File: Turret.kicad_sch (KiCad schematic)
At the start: 0 parts

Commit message: Update schematic
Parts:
- added Feeder1, L_Flywheel_ESC, R_Flywheel_ESC1, Waterwheel1: ~, symbol Robomaster_Library:motor_speed_controller
- added J1: Conn_01x04_Pin, symbol Connector:Conn_01x04_Pin
- added J12, J2, J4, J6, J8: Conn_01x02_Pin, Connector_AMASS:AMASS_XT30U-F_1x02_P5.0mm_Vertical, symbol Connector:Conn_01x02_Pin
- added J13, J3, J5, J7, J9: Conn_01x02_Pin, Connector_JST:JST_GH_BM02B-GHS-TBT_1x02-1MP_P1.25mm_Vertical, symbol Connector:Conn_01x02_Pin
- added SMM1: ~, symbol Robomaster_Library:SMM
- added pitch_motor2: ~, symbol Robomaster_Library:pitch_motor
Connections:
- new net: J6.1 (Pin_1), Waterwheel1.1 (VIN)
- new net: J6.2 (Pin_2), Waterwheel1.2 (GND)
- new net: J7.1 (Pin_1), Waterwheel1.3 (CANH)
- new net: J7.2 (Pin_2), Waterwheel1.4 (CANL)
- new net: Feeder1.3 (CANH), J5.1 (Pin_1)
- new net: Feeder1.4 (CANL), J5.2 (Pin_2)
- new net: J9.1 (Pin_1), pitch_motor2.3 (CANH)
- new net: J9.2 (Pin_2), pitch_motor2.4 (CANL)
- new net: J13.1 (Pin_1), R_Flywheel_ESC1.3 (CANH)
- new net: J13.2 (Pin_2), R_Flywheel_ESC1.4 (CANL)
- new net: J1.1 (Pin_1), SMM1.1 (AVI_1)
- new net: J1.2 (Pin_2), SMM1.2 (AVI_4)
- new net: J1.3 (Pin_3), SMM1.3 (AVI_3)
- new net: J1.4 (Pin_4), SMM1.2 (AVI_4)
- new net: J3.1 (Pin_1), L_Flywheel_ESC.3 (CANH)
- new net: J3.2 (Pin_2), L_Flywheel_ESC.4 (CANL)
- new net: J2.1 (Pin_1), L_Flywheel_ESC.1 (VIN)
- new net: J2.2 (Pin_2), L_Flywheel_ESC.2 (GND)
- new net: J8.1 (Pin_1), pitch_motor2.1 (PWR)
- new net: J8.2 (Pin_2), pitch_motor2.2 (GND)
- new net: J12.1 (Pin_1), R_Flywheel_ESC1.1 (VIN)
- new net: J12.2 (Pin_2), R_Flywheel_ESC1.2 (GND)
- new net: Feeder1.1 (VIN), J4.1 (Pin_1)
- new net: Feeder1.2 (GND), J4.2 (Pin_2)

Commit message: Added footprint for aviator
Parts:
- J1: footprint (none) -> Robomasters:866319112100004
- renumbered L_Flywheel_ESC to L_Flywheel_ESC1
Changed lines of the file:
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@@
   )
   (symbol (lib_id "Robomaster_Library:motor_speed_controller") (at 248.92 81.28 0) (unit 1)
-    (in_bom yes) (on_board yes) (dnp no) (fields_autoplaced)
+    (in_bom yes) (on_board no) (dnp no) (fields_autoplaced)
     (property "Reference" "Waterwheel1" (at 259.08 88.9 0)
       (effects (font (size 1.27 1.27)) (justify left))
@@
       (effects (font (size 1.27 1.27)))
     )
-    (property "Footprint" "" (at 147.32 62.23 0)
+    (property "Footprint" "Robomasters:866319112100004" (at 147.32 62.23 0)
       (effects (font (size 1.27 1.27)) hide)
     )
@@
   )
   (symbol (lib_id "Robomaster_Library:SMM") (at 181.61 55.88 0) (unit 1)
-    (in_bom yes) (on_board yes) (dnp no) (fields_autoplaced)
+    (in_bom yes) (on_board no) (dnp no) (fields_autoplaced)
     (property "Reference" "SMM1" (at 191.77 63.5 0)
       (effects (font (size 1.27 1.27)) (justify left))
@@
   )
   (symbol (lib_id "Robomaster_Library:motor_speed_controller") (at 191.77 27.94 0) (unit 1)
-    (in_bom yes) (on_board yes) (dnp no) (fields_autoplaced)
-    (property "Reference" "L_Flywheel_ESC" (at 201.93 35.56 0)
+    (in_bom yes) (on_board no) (dnp no) (fields_autoplaced)
+    (property "Reference" "L_Flywheel_ESC1" (at 201.93 35.56 0)
       (effects (font (size 1.27 1.27)) (justify left))
     )
@@
       (project "Turret"
         (path "/84905b3c-2997-4e61-b373-c0062fb72371"
-          (reference "L_Flywheel_ESC") (unit 1)
+          (reference "L_Flywheel_ESC1") (unit 1)
         )
       )
@@
   )
   (symbol (lib_name "pitch_motor_1") (lib_id "Robomaster_Library:pitch_motor") (at 186.69 88.9 0) (unit 1)
-    (in_bom yes) (on_board yes) (dnp no) (fields_autoplaced)
+    (in_bom yes) (on_board no) (dnp no) (fields_autoplaced)
     (property "Reference" "pitch_motor2" (at 194.31 100.33 0)
       (effects (font (size 1.27 1.27)) (justify left))
@@
   )
   (symbol (lib_id "Robomaster_Library:motor_speed_controller") (at 251.46 29.21 0) (unit 1)
-    (in_bom yes) (on_board yes) (dnp no) (fields_autoplaced)
+    (in_bom yes) (on_board no) (dnp no) (fields_autoplaced)
     (property "Reference" "R_Flywheel_ESC1" (at 261.62 36.83 0)
       (effects (font (size 1.27 1.27)) (justify left))
@@
   )
   (symbol (lib_id "Robomaster_Library:motor_speed_controller") (at 248.92 54.61 0) (unit 1)
-    (in_bom yes) (on_board yes) (dnp no) (fields_autoplaced)
+    (in_bom yes) (on_board no) (dnp no) (fields_autoplaced)
     (property "Reference" "Feeder1" (at 259.08 62.23 0)
       (effects (font (size 1.27 1.27)) (justify left))

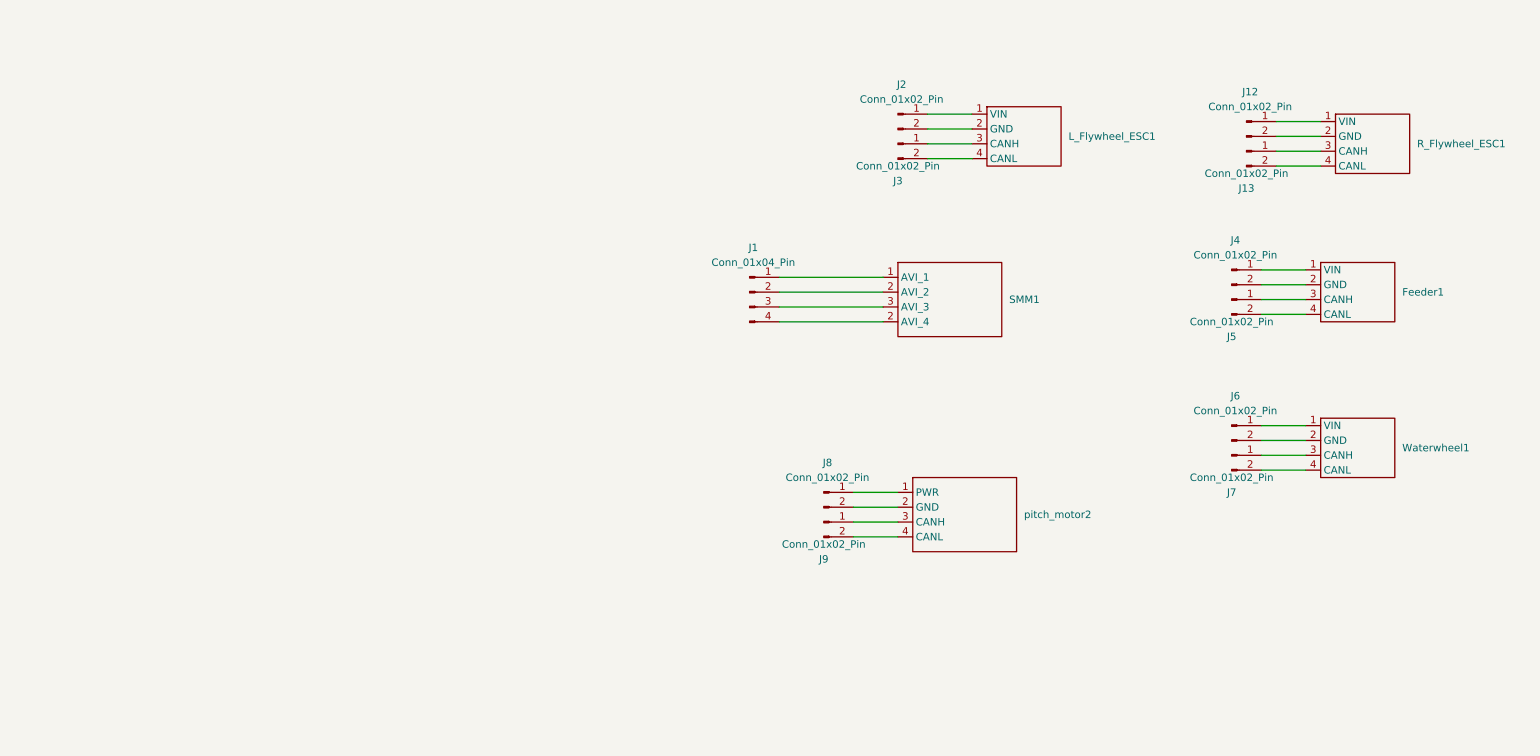
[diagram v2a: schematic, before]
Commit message: Wired to connector
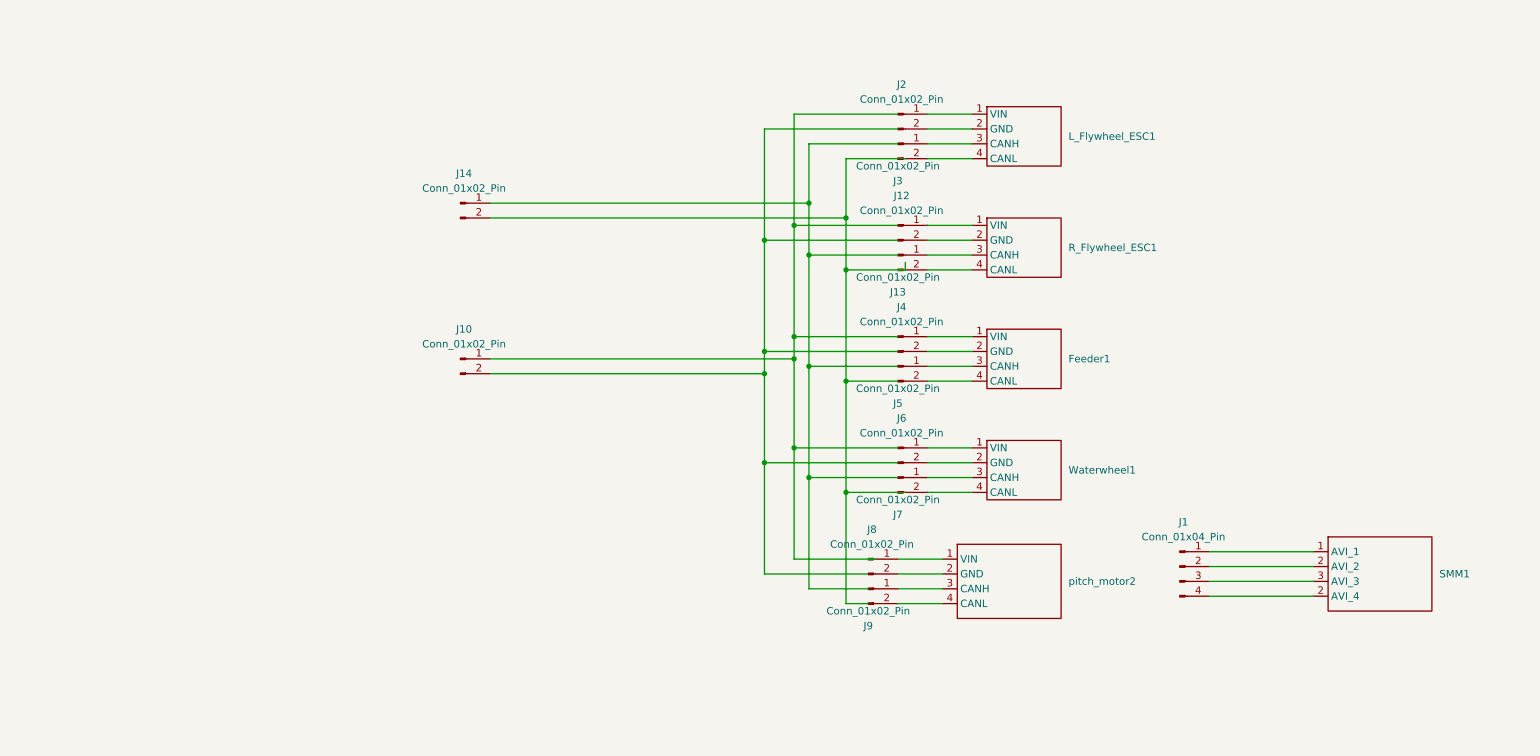
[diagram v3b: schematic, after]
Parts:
- added J10, J14: Conn_01x02_Pin, symbol Connector:Conn_01x02_Pin
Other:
- moved on the sheet: Feeder1, J1, J12, J13, J4, J5, J6, J7, J8, J9, R_Flywheel_ESC1, SMM1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

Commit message: added power connector
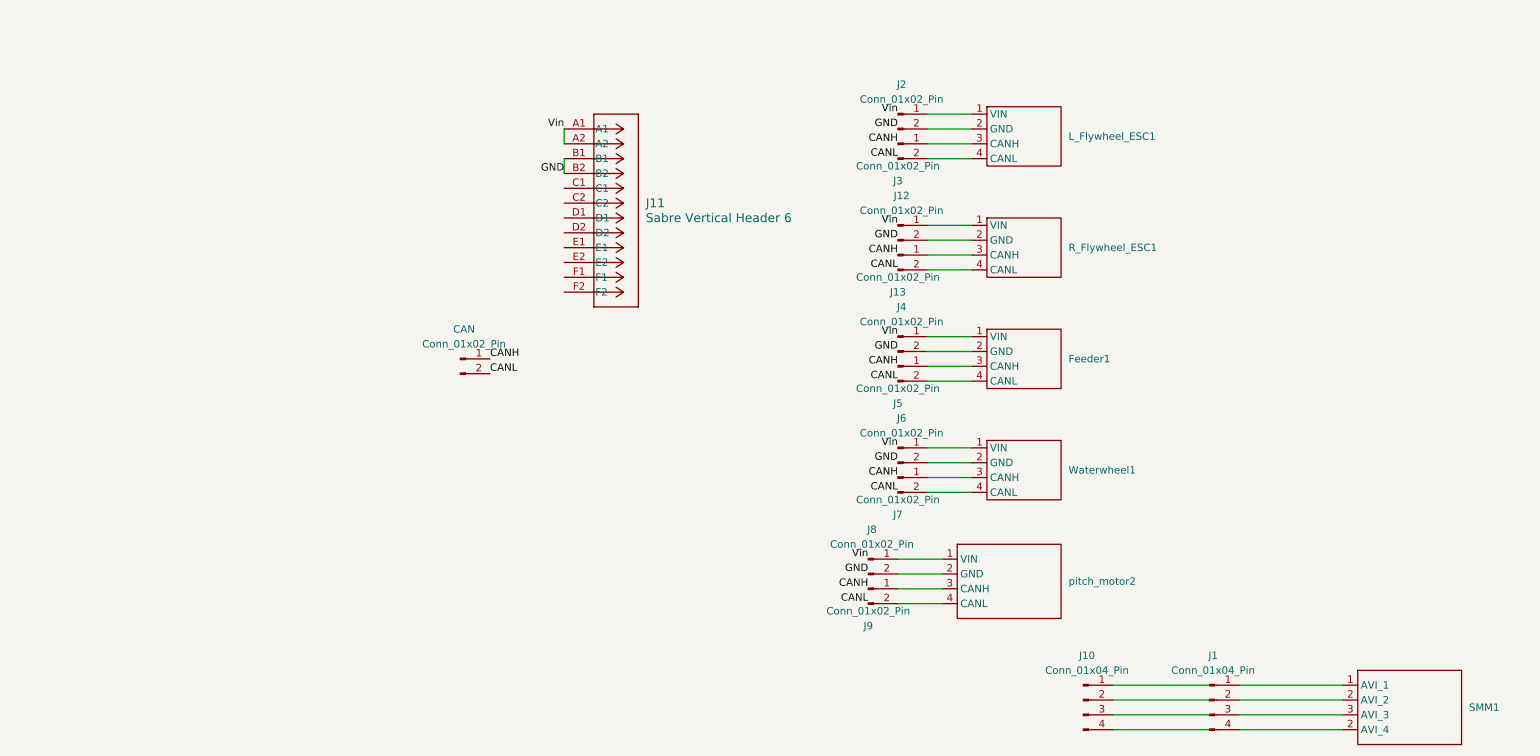
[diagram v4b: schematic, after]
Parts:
- removed J14: Conn_01x02_Pin, symbol Connector:Conn_01x02_Pin
- added J10: Conn_01x04_Pin, Robomasters:866319112100004, symbol Connector:Conn_01x04_Pin
- added J11: Sabre Vertical Header 6, CON_431600106_MOL, symbol Robomaster_Library:Sabre Vertical Header 6
- CAN: renamed from J10; footprint (none) -> Connector_JST:JST_GH_BM02B-GHS-TBT_1x02-1MP_P1.25mm_Vertical
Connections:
- net CANH: now reaches CAN.1 (Pin_1)
- net CANL: now reaches CAN.2 (Pin_2)
- new net GND: J11.B1, J11.B2
- new net Vin: J11.A1, J11.A2
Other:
- moved on the sheet: J1, SMM1

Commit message: Update turret
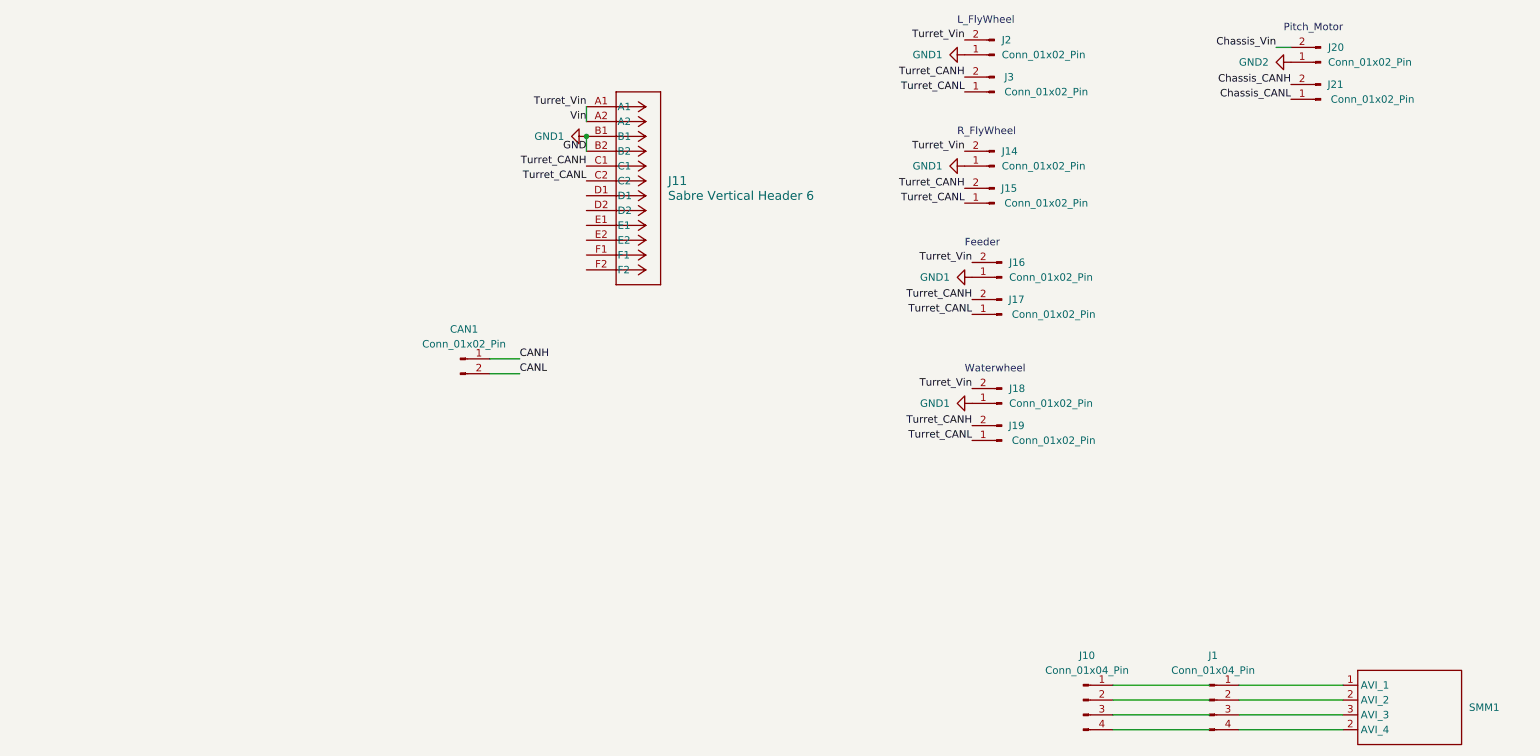
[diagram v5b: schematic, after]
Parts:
- removed Feeder1, L_Flywheel_ESC1, R_Flywheel_ESC1, Waterwheel1: ~, symbol Robomaster_Library:motor_speed_controller
- removed J12, J4, J6, J8: Conn_01x02_Pin, Connector_AMASS:AMASS_XT30U-F_1x02_P5.0mm_Vertical, symbol Connector:Conn_01x02_Pin
- removed J13, J5, J7, J9: Conn_01x02_Pin, Connector_JST:JST_GH_BM02B-GHS-TBT_1x02-1MP_P1.25mm_Vertical, symbol Connector:Conn_01x02_Pin
- removed pitch_motor2: ~, symbol Robomaster_Library:pitch_motor
- added J14, J16, J18, J20: Conn_01x02_Pin, Connector_AMASS:AMASS_XT30U-F_1x02_P5.0mm_Vertical, symbol Connector:Conn_01x02_Pin
- added J15, J17, J19, J21: Conn_01x02_Pin, Connector_JST:JST_GH_BM02B-GHS-TBT_1x02-1MP_P1.25mm_Vertical, symbol Connector:Conn_01x02_Pin
- renumbered CAN to CAN1
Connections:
- net GND is gone; now on net GND1: J11.B1, J11.B2
- net Vin is gone; now on net Turret_Vin: J11.A1, J11.A2
- net Turret_CANL: now reaches J3.1 (Pin_1)
- net Turret_CANL: now also J11.C2, J15.1 (Pin_1), J17.1 (Pin_1), J19.1 (Pin_1)
- net Turret_CANH: now reaches J3.2 (Pin_2)
- net Turret_CANH: now also J11.C1, J15.2 (Pin_2), J17.2 (Pin_2), J19.2 (Pin_2)
- net GND1: now reaches J2.1 (Pin_1)
- net GND1: now also J14.1 (Pin_1), J16.1 (Pin_1), J18.1 (Pin_1)
- net Turret_Vin: now reaches J2.2 (Pin_2)
- net Turret_Vin: now also J14.2 (Pin_2), J16.2 (Pin_2), J18.2 (Pin_2)
- new net Chassis_CANH: J21.2 (Pin_2)
- new net Chassis_CANL: J21.1 (Pin_1)
- new net Chassis_Vin: J20.2 (Pin_2)
- new net GND2: J20.1 (Pin_1)
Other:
- note added: "Feeder"
- note added: "L_FlyWheel"
- note added: "Pitch_Motor"
- note added: "R_FlyWheel"
- note added: "Waterwheel"
- moved on the sheet: J11, J2, J3

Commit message: Updated PCB to use unified power 6 pin, added 2 1x2 connectors
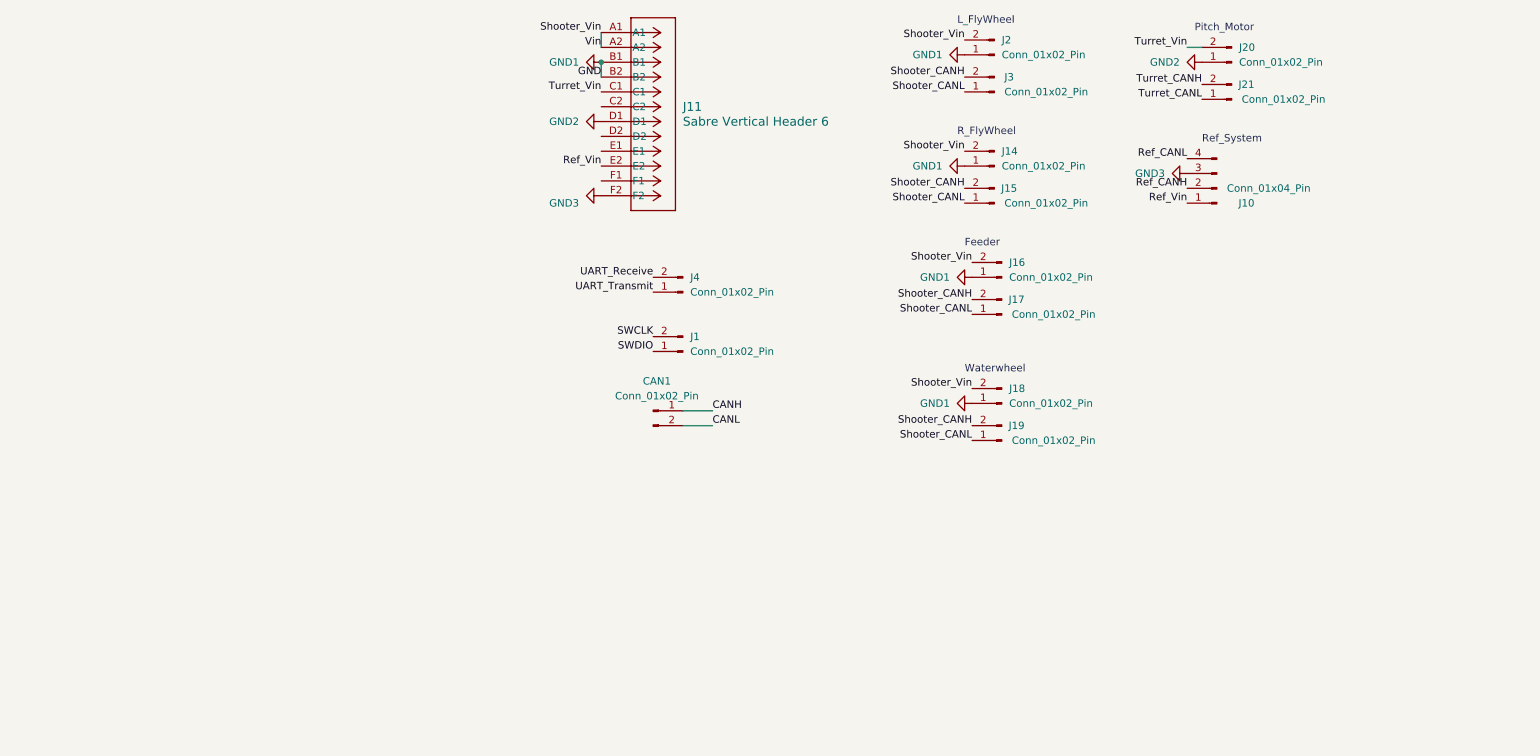
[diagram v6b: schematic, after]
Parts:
- removed J1: Conn_01x04_Pin, Robomasters:866319112100004, symbol Connector:Conn_01x04_Pin
- removed SMM1: ~, symbol Robomaster_Library:SMM
- added J1, J4: Conn_01x02_Pin, symbol Connector:Conn_01x02_Pin
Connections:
- net Chassis_CANH is gone; now on net Turret_CANH: J21.2 (Pin_2)
- net Chassis_CANL is gone; now on net Turret_CANL: J21.1 (Pin_1)
- net Chassis_Vin is gone; now on net Turret_Vin: J20.2 (Pin_2)
- net GND2: now also J11.D1
- net Turret_CANH: no longer J11.C1, J15.2 (Pin_2), J17.2 (Pin_2), J19.2 (Pin_2), J3.2 (Pin_2)
- net Turret_CANL: no longer J11.C2, J15.1 (Pin_1), J17.1 (Pin_1), J19.1 (Pin_1), J3.1 (Pin_1)
- net Turret_Vin: now also J11.C1; no longer J11.A1, J11.A2, J14.2 (Pin_2), J16.2 (Pin_2), J18.2 (Pin_2), J2.2 (Pin_2)
- net Ref_Vin: now reaches J10.1 (Pin_1)
- net Ref_Vin: now also J11.E2
- net Ref_CANH: now reaches J10.2 (Pin_2)
- net GND3: now reaches J10.3 (Pin_3)
- net GND3: now also J11.F2
- net Ref_CANL: now reaches J10.4 (Pin_4)
- new net SWCLK: J1.2 (Pin_2)
- new net SWDIO: J1.1 (Pin_1)
- new net Shooter_CANH: J15.2 (Pin_2), J17.2 (Pin_2), J19.2 (Pin_2), J3.2 (Pin_2)
- new net Shooter_CANL: J15.1 (Pin_1), J17.1 (Pin_1), J19.1 (Pin_1), J3.1 (Pin_1)
- new net Shooter_Vin: J11.A1, J11.A2, J14.2 (Pin_2), J16.2 (Pin_2), J18.2 (Pin_2), J2.2 (Pin_2)
- new net UART_Receive: J4.2 (Pin_2)
- new net UART_Transmit: J4.1 (Pin_1)
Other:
- note added: "Ref_System"
- moved on the sheet: CAN1, J10, J11, J20, J21

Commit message: Mostly finished turret schematic
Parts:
- removed J1: Conn_01x02_Pin, symbol Connector:Conn_01x02_Pin
- removed J14, J16, J18: Conn_01x02_Pin, Connector_AMASS:AMASS_XT30U-F_1x02_P5.0mm_Vertical, symbol Connector:Conn_01x02_Pin
- removed J15, J17, J19: Conn_01x02_Pin, Connector_JST:JST_GH_BM02B-GHS-TBT_1x02-1MP_P1.25mm_Vertical, symbol Connector:Conn_01x02_Pin
- added H1, H2, H3, H4: MountingHole, MountingHole:MountingHole_3mm, symbol Mechanical:MountingHole
- added J1, J5: Conn_01x04_Pin, symbol Connector:Conn_01x04_Pin
- added J12, J6, J8: Conn_01x02_Pin, Connector_JST:JST_GH_BM02B-GHS-TBT_1x02-1MP_P1.25mm_Vertical, symbol Connector:Conn_01x02_Pin
- added J7, J9: Conn_01x02_Pin, Connector_AMASS:AMASS_XT30U-F_1x02_P5.0mm_Vertical, symbol Connector:Conn_01x02_Pin
- J11: footprint CON_431600106_MOL -> (none)
- J4: footprint (none) -> Connector_AMASS:AMASS_XT30U-F_1x02_P5.0mm_Vertical
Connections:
- net UART_Transmit is gone; now on net GND: J4.1 (Pin_1)
- net GND2: no longer J20.1 (Pin_1)
- net GND3: no longer J10.3 (Pin_3)
- net SWCLK: now also J5.3 (Pin_3)
- net SWDIO: now also J5.2 (Pin_2)
- net Shooter_CANH: now also J12.2 (Pin_2), J6.2 (Pin_2), J8.2 (Pin_2)
- net Shooter_CANL: now also J12.1 (Pin_1), J6.1 (Pin_1), J8.1 (Pin_1)
- net Shooter_Vin: no longer J2.2 (Pin_2)
- net Turret_Vin: no longer J20.2 (Pin_2)
- net GND1 renamed GND
- net GND: now also J10.3 (Pin_3), J20.1 (Pin_1), J1.1 (Pin_1), J5.1 (Pin_1), J7.1 (Pin_1), J9.1 (Pin_1)
- net UART_Receive renamed +24V
- net +24V: now also J2.2 (Pin_2), J20.2 (Pin_2), J7.2 (Pin_2), J9.2 (Pin_2)
- new net +3.3V: J1.4 (Pin_4), J5.4 (Pin_4)
- new net UART_RX: J1.3 (Pin_3)
- new net UART_TX: J1.2 (Pin_2)
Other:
- note added: "Mounting Holes"
- note added: "Remote Debug Connector Orin -> Devboard"
- note added: "Shooter"
- note added: "UART Connection Orin -> Devboard"
- moved on the sheet: CAN1, J10, J11, J20, J21
